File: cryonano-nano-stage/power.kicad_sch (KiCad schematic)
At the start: 1 part, among them J1 Conn_01x03_Pin

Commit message: preliminary components added
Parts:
- removed J1: Conn_01x03_Pin, symbol Connector:Conn_01x03_Pin
- added C1: 100uF, Capacitor_THT:CP_Radial_D8.0mm_P3.50mm, symbol Device:C_Polarized_Small_US
- added C3: 10uF, Capacitor_SMD:C_1210_3225Metric, symbol Device:C_Small
- added C4: 10u, Capacitor_SMD:C_1206_3216Metric, symbol Device:C_Small
- added C65: 1nF, Capacitor_THT:C_Disc_D9.0mm_W5.0mm_P10.00mm, symbol Device:C_Small
- added D11: SMBJ30CA, Diode_SMD:D_SMB, symbol symbols:SMBJ30CA/TR13
- added D2, D4: BAT760, Diode_SMD:D_SOD-323, symbol symbols:BAT760
- added D8: PESD12VL1BA, Diode_SMD:D_SOD-323F, symbol symbols:PESD12VL1BA,115
- added F1: FMC16302WBTP, FUSC1608X55N, symbol symbols:FMC16302WBTP
- added FL2: ACM4520-142-2P-T000, footprints:ACM45204212PT000, symbol symbols:ACM4520-142-2P-T000
- added GD1: B32-150-LF, footprints:B32_GDT_YAGEO, symbol symbols:B32-150-LF
- added MOV1: 560KD07, Varistor:RV_Disc_D9mm_W4.8mm_P5mm, symbol symbols:560KD07
- added Q1: PMV100EPAR, footprints:SOT95P230X110-3N, symbol symbols:PMV100EPAR
- added R1: 10k, Resistor_SMD:R_0603_1608Metric, symbol Device:R_Small
- added R26: 1M, Resistor_THT:R_Axial_DIN0207_L6.3mm_D2.5mm_P10.16mm_Horizontal, symbol Device:R_Small
- added TP1, TP4: +5V0_1, footprints:TestPoint_THTPad_D1.3mm_Drill0.8mm, symbol Connector:TestPoint
- added TP2, TP3: TestPoint, footprints:TestPoint_THTPad_D1.3mm_Drill0.8mm, symbol Connector:TestPoint
- added U4: AP7363-33D-13, footprints:TO252__DPAK__1, symbol symbols:AP7363-33D-13
- added Z1: PDZ15B, footprints:SOD2512X110N, symbol base_6in_24out_components:PDZ15B,115
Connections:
- new net: D11.1, F1.2, FL2.1, GD1.1, MOV1.1
- new net: FL2.4, Q1.3 (D)
- new net: Q1.1 (G), R1.1, Z1.2 (A)
- new net +24V0: C1.1, C3.1, C4.1, Q1.2 (S), TP2.1, Z1.1 (K)
- new net +24V0IN: F1.1
- new net +3V3_OUT_3: TP4.1, U4.2 (OUT)
- new net +5V0_OUT_2: D2.1 (K), D4.1 (K), TP1.1, U4.1 (IN)
- new net 0V0: C1.2, C3.2, C4.2, C65.1, D8.2, FL2.3, R1.2, R26.1, TP3.1
- new net 0V0IN: D11.2, FL2.2, GD1.2, MOV1.2
- new net 0V0_OUT_2: U4.3 (GND)
- new net Buck converter 2/+5V0OUT: D2.2 (A)
- new net Earth: C65.2, D8.1, R26.2
- new net V_BUS: D4.2 (A)
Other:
- added sheet Buck converter 1 (buck-converter-1.kicad_sch)
- added sheet Buck converter 2 (buck-converter-2.kicad_sch)
- note added: "ESD"

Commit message: sch updated
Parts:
- FL2: Unit Price 10 109 -> 71
- U4: Order No. (none) -> AP7363-33D-13; Unit Price 10 (none) -> 27
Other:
- note added: "EMC and Surge Handling"
- note added: "ESD Protection"
- note added: "Gate driver supply"
- note added: "MCU and ADC supply"
- note added: "Note: Incoming from USB 5V."
- note added: "Reverse polarity protection"
- note added: "Ripple handling"
- note removed: "ESD"
- moved on the sheet: C1, C3, C4, C65, D11, D2, D4, D8, F1, FL2, GD1, MOV1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

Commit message: sch improved
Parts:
- added PS2: B2405S-1WR3, SamacSys_Parts:HLKB2405S2WR3, symbol symbols:BxxxxS-1WR3
- added PS4: B2405S-2WR3, symbol symbols:BxxxxS-2WR3
- C1: value 100uF -> 100u
- C3: value 10uF -> 10u; footprint Capacitor_SMD:C_1210_3225Metric -> Capacitor_SMD:C_1206_3216Metric; Order No. CL32B106KBJNNNE -> (none); Unit Price 10 18.5 -> (none)
- C4: Source in.element14.com -> (none); Unit Price 10 16 -> (none)
- C65: value 1nF -> 1n
- R1: Order No. CRCW060310K0FKEE -> (none); Unit Price 10 2.6 -> (none)
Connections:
- net 0V0 is gone; now on net 0V0_OUT_1: C1.2, C3.2, C4.2, C65.1, D8.2, FL2.3, R1.2, R26.1, TP3.1
- net 0V0_OUT_1: now also PS2.1 (GND), PS4.2 (GND)
- net 0V0_OUT_2: now also PS2.3 (-VO), PS4.4 (-VOUT)
- net +24V0 renamed +24V0_OUT_1
- net +24V0_OUT_1: now also PS2.2 (+VIN), PS4.1 (+VIN)
- net Buck converter 2/+5V0OUT renamed +5V0
- net +5V0: now also PS2.4 (+VO), PS4.6 (+VOUT)
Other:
- removed sheet Buck converter 1
- removed sheet Buck converter 2
- note removed: "Gate driver supply"
- company: (none) -> Cryonano Labs Pvt. Ltd.
- title: (none) -> Nano stage controller
- moved on the sheet: C1, C3, C65, D11, D2, D4, D8, F1, FL2, GD1, MOV1, Q1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

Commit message: sch improved
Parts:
- PS2: value B2405S-1WR3 -> BxxxxS-1WR3; footprint SamacSys_Parts:HLKB2405S2WR3 -> footprints:BxxxxS-1WR3
- PS4: value B2405S-2WR3 -> BxxxxS-2WR3; footprint (none) -> footprints:BxxxxS-2WR3

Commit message: sch improved
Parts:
- removed TP2, TP3: TestPoint, footprints:TestPoint_THTPad_D1.3mm_Drill0.8mm, symbol Connector:TestPoint
- added C5: 10n, Capacitor_SMD:C_1206_3216Metric, symbol Device:C_Small
- added C6: 1u, Capacitor_SMD:C_0805_2012Metric, symbol Device:C_Small
- added C7, C8: 10u, Capacitor_SMD:C_0805_2012Metric, symbol Device:C_Small
- added TP2: 24V RAW, Connector_PinSocket_2.54mm:PinSocket_1x02_P2.54mm_Vertical, symbol Connector:Conn_01x02_Socket
- C65, D8, R26: now fitted; now in the parts list
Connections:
- net +24V0_OUT_1: now also C6.1, TP2.1 (Pin_1)
- net +3V3_OUT_3: now also C8.1
- net +5V0_OUT_2: now also C7.1
- net 0V0IN: now also C5.2
- net 0V0_OUT_1: now also C6.2, TP2.2 (Pin_2)
- net 0V0_OUT_2: now also C7.2, C8.2
- net at D11.1, F1.2, FL2.1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: now also C5.1
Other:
- moved on the sheet: D11, F1, GD1, MOV1

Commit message: pcb drc ok. 68 ohm matching pending
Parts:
- removed TP2: 24V RAW, Connector_PinSocket_2.54mm:PinSocket_1x02_P2.54mm_Vertical, symbol Connector:Conn_01x02_Socket
- added TP5: 1x02 2.54mm, Connector_PinSocket_2.54mm:PinSocket_1x02_P2.54mm_Vertical, symbol Connector:Conn_01x02_Socket
- C1: Manufacturer (none) -> KEMET; Order No. (none) -> ESL107M050AGMAA; Unit Price 10 (none) -> 16; Voltage 63V -> 50V
- C3, C4: footprint Capacitor_SMD:C_1206_3216Metric -> Capacitor_SMD:C_1210_3225Metric; Manufacturer (none) -> YAGEO; Order No. (none) -> CC1210KFX7R9BB106; Unit Price 10 (none) -> 31.1
- C5: Manufacturer (none) -> MURATA; Order No. (none) -> GRT3195C2A103JA02D; Unit Price 10 (none) -> 11
- C6: Manufacturer (none) -> MURATA; Order No. (none) -> GCM21BR71H105KA03K; Unit Price 10 (none) -> 9.2
- C65: footprint Capacitor_THT:C_Disc_D9.0mm_W5.0mm_P10.00mm -> Capacitor_THT:C_Disc_D9.0mm_W5.0mm_P7.50mm; Order No. (none) -> CK45-B3FD102KYGNA; Unit Price 10 (none) -> 39
- C7, C8: footprint Capacitor_SMD:C_0805_2012Metric -> Capacitor_SMD:C_1206_3216Metric; Manufacturer (none) -> KEMET; Order No. (none) -> C1206C106K4RACTU; Unit Price 10 (none) -> 13.5
- F1: footprint FUSC1608X55N -> footprints:FUSC1608X55N; Manufacturer_Name Kamaya -> (none); Manufacturer_Part_Number FMC16302WBTP -> (none); Mouser Part Number 791-FMC16302WBTP -> (none); Mouser Price/Stock https://www.mouser.co.uk/ProductDetail/Kamaya/FMC16302WBTP?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 -> (none)
- FL2: Manufacturer_Name TDK -> (none); Manufacturer_Part_Number ACM4520-142-2P-T000 -> (none); Mouser Part Number 810-ACM45201422PT000 -> (none); Mouser Price/Stock https://www.mouser.co.uk/ProductDetail/TDK/ACM4520-142-2P-T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 -> (none)
- Q1: Arrow Part Number PMV100EPAR -> (none); Arrow Price/Stock https://www.arrow.com/en/products/pmv100epar/nexperia?utm_c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 -> (none); Manufacturer_Name Nexperia -> (none); Manufacturer_Part_Number PMV100EPAR -> (none); Mouser Part Number 771-PMV100EPAR -> (none); Mouser Price/Stock https://www.mouser.co.uk/ProductDetail/Nexperia/PMV100EPAR?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 -> (none)
- U4: Manufacturer_Name Diodes Incorporated -> (none); Manufacturer_Part_Number AP7363-33D-13 -> (none)
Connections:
- net +24V0_OUT_1: now also TP5.1 (Pin_1)
- net 0V0_OUT_1: now also TP5.2 (Pin_2)

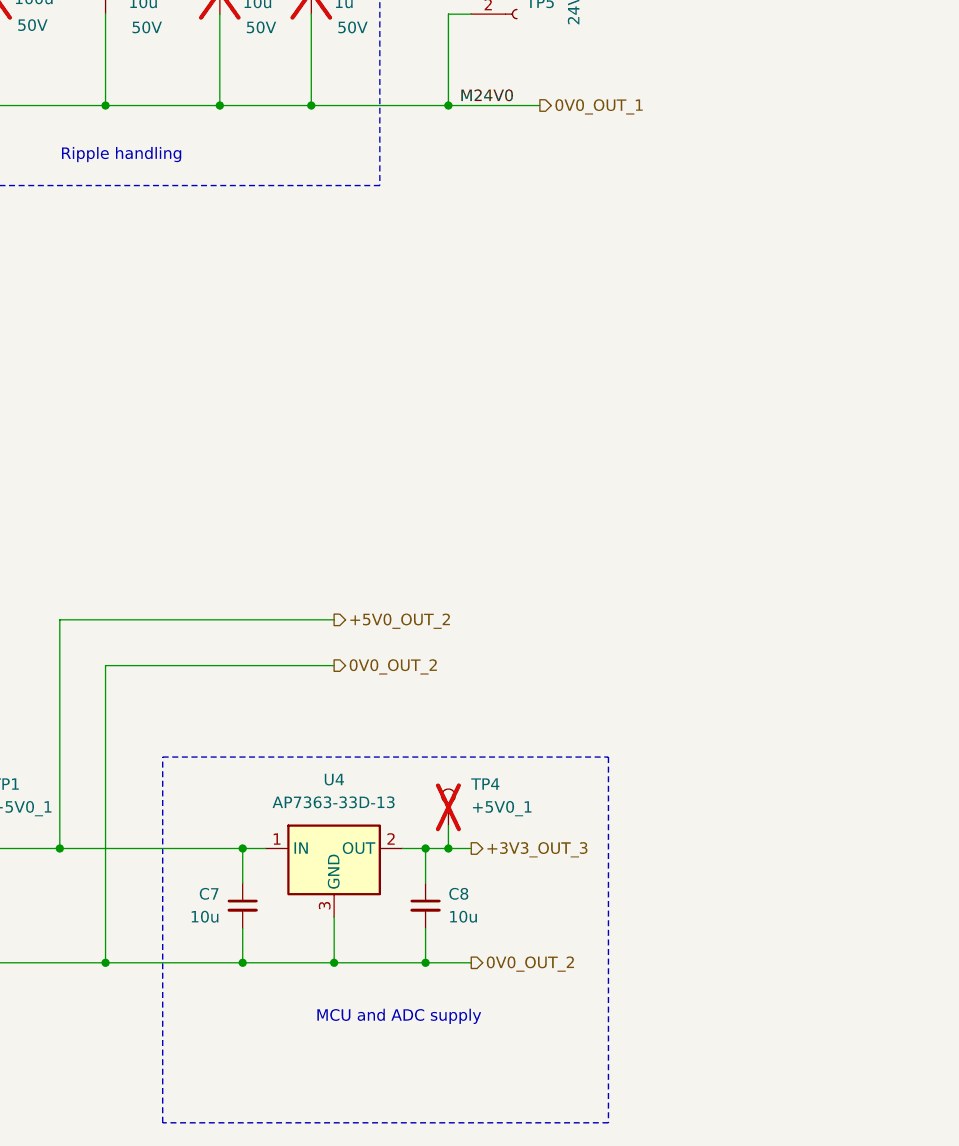
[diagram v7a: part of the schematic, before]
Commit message: drc no error, only warnings
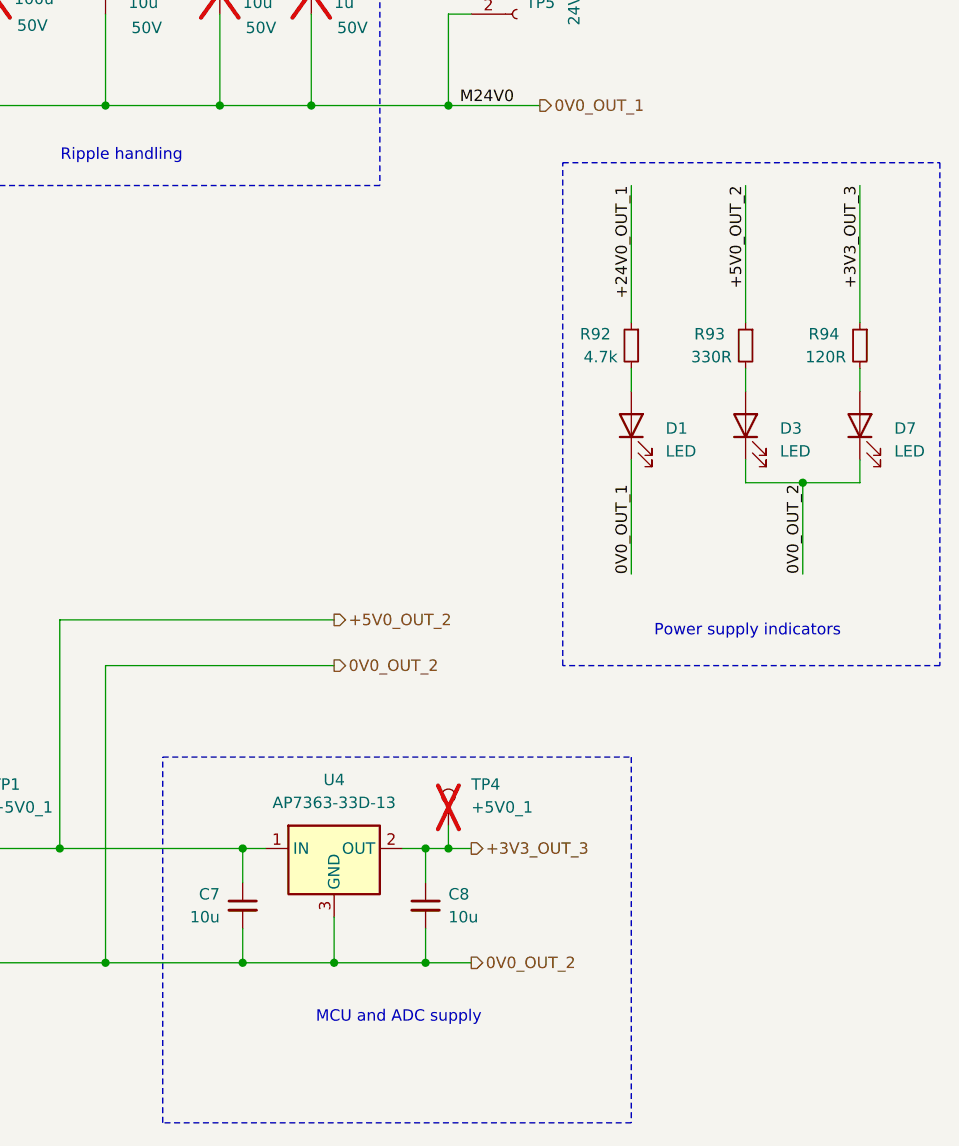
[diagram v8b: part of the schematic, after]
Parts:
- added D1, D3, D7: LED, LED_SMD:LED_0603_1608Metric_Pad1.05x0.95mm_HandSolder, symbol Device:LED
- added R92: 4.7k, Resistor_SMD:R_0603_1608Metric, symbol Device:R_Small
- added R93: 330R, Resistor_SMD:R_0603_1608Metric, symbol Device:R_Small
- added R94: 120R, Resistor_SMD:R_0603_1608Metric, symbol Device:R_Small
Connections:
- net +24V0_OUT_1: now also R92.1
- net +3V3_OUT_3: now also R94.1
- net +5V0_OUT_2: now also R93.1
- net 0V0_OUT_1: now also D1.1 (K)
- net 0V0_OUT_2: now also D3.1 (K), D7.1 (K)
- new net: D1.2 (A), R92.2
- new net: D3.2 (A), R93.2
- new net: D7.2 (A), R94.2
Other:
- note added: "Power supply indicators"
